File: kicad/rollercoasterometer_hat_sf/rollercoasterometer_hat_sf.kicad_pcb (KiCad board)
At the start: 2 copper layers, 65 x 87.8 mm, 66 parts, among them J101 Raspberry_Pi_40, J102 Conn_01x03, J103 LSD9DS1, J104 ICM20948, J105 BME680, J201 SMA, J202 NormallyClosed, J301 USB_C_Receptacle, J302 USB_C_Receptacle, U1201 LPC2103, U1401 74LS138, U1402 TXS0108, U1601 ICM-42688, U1701 BMM150, U1801 AK09918, U1901 BMP384, U201 ZED_F9R, U401 TCR2EF 3.3V, U501 TCR2EF 1.8V, Y1201 12MHz

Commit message: Commit as-ordered shipometer 23.03
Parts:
- removed C1605: 10nF, Capacitor_SMD:C_0402_1005Metric
- removed C1606: 2.2uF, Capacitor_SMD:C_0402_1005Metric
- removed C1608, C1722, C1755, C1811, C1901, C1910: 100nF, Capacitor_SMD:C_0402_1005Metric
- removed D302: RED, LED_SMD:LED_0603_1608Metric
- removed G1501: Axis, KwanSystems:Axis
- removed G1502, G1505: KwanSystems, KwanSystems:StKwansSoldermask
- removed G1503, G1507: DesignedWithKicad, KwanSystems:Symbol_KiCAD-Logo_CopperAndSilkScreenTop_small
- removed G1504, G1506: OSHW, KwanSystems:OSHW-Symbol_6.7x6mm_SolderMask
- removed J302: USB_C_Receptacle, KwanSystems:USB_C_Amphenol_MidMount_with_cutout
- removed U1402: TXS0108, Package_SO:TSSOP-20_4.4x6.5mm_P0.65mm
- removed U1601: ICM-42688, KwanSystems:QFN50P300X250X97-14N
- removed U1701: BMM150, KwanSystems:BMM150
- removed U1801: AK09918, KwanSystems:AK09918C
- removed U1901: BMP384, KwanSystems:BMP384
- added D101: White, LED_SMD:LED_0603_1608Metric, F.Cu at (208.0, 55.9)
- added D102: White, LED_SMD:LED_0603_1608Metric, F.Cu at (208.0, 57.7)
- added D103: White, LED_SMD:LED_0603_1608Metric, F.Cu at (208.0, 59.4)
- added D104: White, LED_SMD:LED_0603_1608Metric, F.Cu at (208.0, 61.2)
- added D1206: Blue, LED_SMD:LED_0603_1608Metric, F.Cu at (208.0, 64.8)
- added D1229: Red, LED_SMD:LED_0603_1608Metric, F.Cu at (208.0, 70.1)
- added D1230: Green, LED_SMD:LED_0603_1608Metric, F.Cu at (208.0, 68.3)
- added D1241: Yellow, LED_SMD:LED_0603_1608Metric, F.Cu at (208.0, 63.0)
- added D1244: Yellow, LED_SMD:LED_0603_1608Metric, F.Cu at (208.0, 66.5)
- added R1229: 68, Resistor_SMD:R_0402_1005Metric, F.Cu at (201.7, 71.4)
- added R1241: 68, Resistor_SMD:R_0402_1005Metric, F.Cu at (201.7, 63.0)
- added R1244: 68, Resistor_SMD:R_0402_1005Metric, F.Cu at (201.7, 68.3)
- D301: value RED -> USBLC6-4SC6; footprint LED_SMD:LED_0603_1608Metric -> Package_TO_SOT_SMD:SOT-23-6
- G103, G107: value DesignedWithKicad -> Designed with
- J103: value LSD9DS1 -> LSM9DS1
- J202: footprint KwanSystems:SolderJumper-2_P1.3mm_MaskBridged_RoundedPad1.0x1.5mm -> Jumper:SolderJumper-2_P1.3mm_Bridged_RoundedPad1.0x1.5mm
- moved U102 38.9 mm to (159.3, 59.2)
- moved C401 19.8 mm to (177.4, 70.2), turned to 90 degrees
- moved U401 17.5 mm to (174.6, 70.2), turned to 180 degrees
- moved C405 15.8 mm to (171.8, 70.2), turned to 90 degrees
- moved D301 8.76 mm to (177.5, 87.9), turned to -90 degrees
- moved R302 2.03 mm to (175.5, 92.2)
- moved C1240 0.79 mm to (163.6, 58.4)
- moved G103 0.36 mm to (208.5, 93.5)
- moved G107 0.36 mm to (208.5, 93.5)
- renumbered U1401 to U102
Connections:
- C1217 pad 1: +1V8 -> +3V3
- C1240 pad 1: +1V8 -> +3V3
- D301 pad 1: GND -> unconnected-(D301-Pad1)
- D301 pad 2: /P_RET_1V8 -> GND
- J101 pad 10: /GPS_TX -> /LPC_TX
- J101 pad 11: /LPC_~{RESET} -> /CS_A2
- J101 pad 13: unconnected-(J101-Pad13) -> /CS_A1
- J101 pad 15: unconnected-(J101-Pad15) -> /CS_A0
- J101 pad 16: unconnected-(J101-Pad16) -> /LPC_~{RESET}
- J101 pad 18: unconnected-(J101-Pad18) -> /LPC_~{BOOTSTRAP}
- J101 pad 22: unconnected-(J101-Pad22) -> /DRDY_MAG
- J101 pad 29: unconnected-(J101-Pad29) -> /GPS_RX
- J101 pad 31: unconnected-(J101-Pad31) -> /DRDY_6D
- J101 pad 32: /LPC_RX -> unconnected-(J101-Pad32)
- J101 pad 33: /LPC_TX -> unconnected-(J101-Pad33)
- J101 pad 35: /CS1 -> unconnected-(J101-Pad35)
- J101 pad 37: /CS0 -> unconnected-(J101-Pad37)
- J101 pad 7: unconnected-(J101-Pad7) -> /GPS_TX
- J101 pad 8: /GPS_RX -> /LPC_RX
- J301 pad A11: /USB+ Cable/P_INT2 -> unconnected-(J301-PadA11)
- J301 pad A2: /SDA_LPC_1V8 -> unconnected-(J301-PadA2)
- J301 pad A5: /USB+ Cable/P_CC1 -> /USB C Cable/P_CC1
- J301 pad A8: +1V8 -> unconnected-(J301-PadA8)
- J301 pad B10: /SCL_LPC_1V8 -> unconnected-(J301-PadB10)
- J301 pad B11: /P_RET_1V8 -> unconnected-(J301-PadB11)
- J301 pad B2: /USB+ Cable/P_INT3 -> unconnected-(J301-PadB2)
- J301 pad B3: /SHOE_INT_1V8 -> unconnected-(J301-PadB3)
- J301 pad B5: /USB+ Cable/P_CC2 -> /USB C Cable/P_CC2
- J301 pad S1: GND -> unconnected-(J301-PadS1)
- R301 pad 2: /USB+ Cable/P_CC2 -> /USB C Cable/P_CC1
- R302 pad 2: /USB+ Cable/P_CC1 -> /USB C Cable/P_CC2
- U102 pad 1: /CS0 -> /CS_A0
- U102 pad 2: /CS1 -> /CS_A1
- U102 pad 3: GND -> /CS_A2
- U1201 pad 10: /Timer/CAP2.2 -> unconnected-(U1201-Pad10)
- U1201 pad 18: /SCL_LPC_3V3 -> /Timer/SCL0
- U1201 pad 21: /SDA_LPC_3V3 -> /Timer/SDA0
- U1201 pad 29: unconnected-(U1201-Pad29) -> /Timer/DRDY
- U1201 pad 30: unconnected-(U1201-Pad30) -> /Timer/DRDY_MAG_ECHO
- U1201 pad 4: +1V8 -> +3V3
- U1201 pad 41: unconnected-(U1201-Pad41) -> /Timer/PPS-
- U1201 pad 44: /Timer/~{BOOTSTRAP} -> /LPC_~{BOOTSTRAP}
- U1201 pad 48: /SHOE_INT_3V3 -> /Timer/CAP1.3
- U1201 pad 8: /PPS -> unconnected-(U1201-Pad8)
- U1201 pad 9: /Timer/CAP2.1 -> unconnected-(U1201-Pad9)
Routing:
- net +3V3: track 40.5 -> 210.7 mm, vias 4 -> 6
- net /~{CS}_6D: track 0.00 -> 96.8 mm, vias 0 -> 5
- net /MOSI_3V3: track 0.00 -> 95.6 mm, vias 0 -> 3
- net /MISO_3V3: track 0.00 -> 84.9 mm, vias 0 -> 1
- net /~{CS}_MAG: track 0.00 -> 83.7 mm, vias 0 -> 2
- net /SCK_3V3: track 0.00 -> 79.0 mm
- net /LPC_~{RESET}: track 0.00 -> 68.6 mm, vias 0 -> 4
- net /VBUS: track 0.00 -> 66.4 mm, vias 0 -> 5
- net /DRDY_6D: track 0.00 -> 63.0 mm, vias 0 -> 6
- net /DRDY_MAG: track 0.00 -> 60.8 mm, vias 0 -> 3
- net /~{CS}_LPC_3V3: track 0.00 -> 58.6 mm, vias 0 -> 8
- net /LPC_~{BOOTSTRAP}: track 0.00 -> 57.4 mm, vias 0 -> 4
- net /~{CS}_PRES: track 0.00 -> 56.3 mm, vias 0 -> 6
- net /Q_1V8: track 53.5 -> 0.00 mm, vias 2 -> 0
- net /Timer/DRDY_MAG_ECHO: track 0.00 -> 46.5 mm, vias 0 -> 8
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- removed copper zone on B.Cu, net /Q_GND
- removed copper zone on F.Cu, net /Q_GND
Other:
- board size 65 x 87.8 mm -> 65 x 56.5 mm
- board text added: "03 Mar 2023"
- board text added: "Shipometer HAT"
- board text added: "Version 23.03 No Shoe"
- board text removed: "01 Nov 2022"
- board text removed: "Rollercoasterometer HAT"
- board text removed: "Rollercoasterometer Shoe"
- board text removed: "Shoe"
- board text removed: "Version 22.11"
- board text removed: "Version 22.11 01 Nov 2022"

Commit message: Improved grounding and bypass caps on GPS
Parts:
- added C233: 1uF, Capacitor_SMD:C_0402_1005Metric, F.Cu at (166.6, 71.9)
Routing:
- net /Timer/DRDY_MAG_ECHO: track 46.5 -> 56.1 mm, vias 8 -> 9
- net +3V3: track 210.7 -> 212.3 mm
- net /Timer/PPS-: track 41.2 -> 41.9 mm
- net /SCK_3V3: track 79.0 -> 79.6 mm
- net GND: vias 55 -> 62

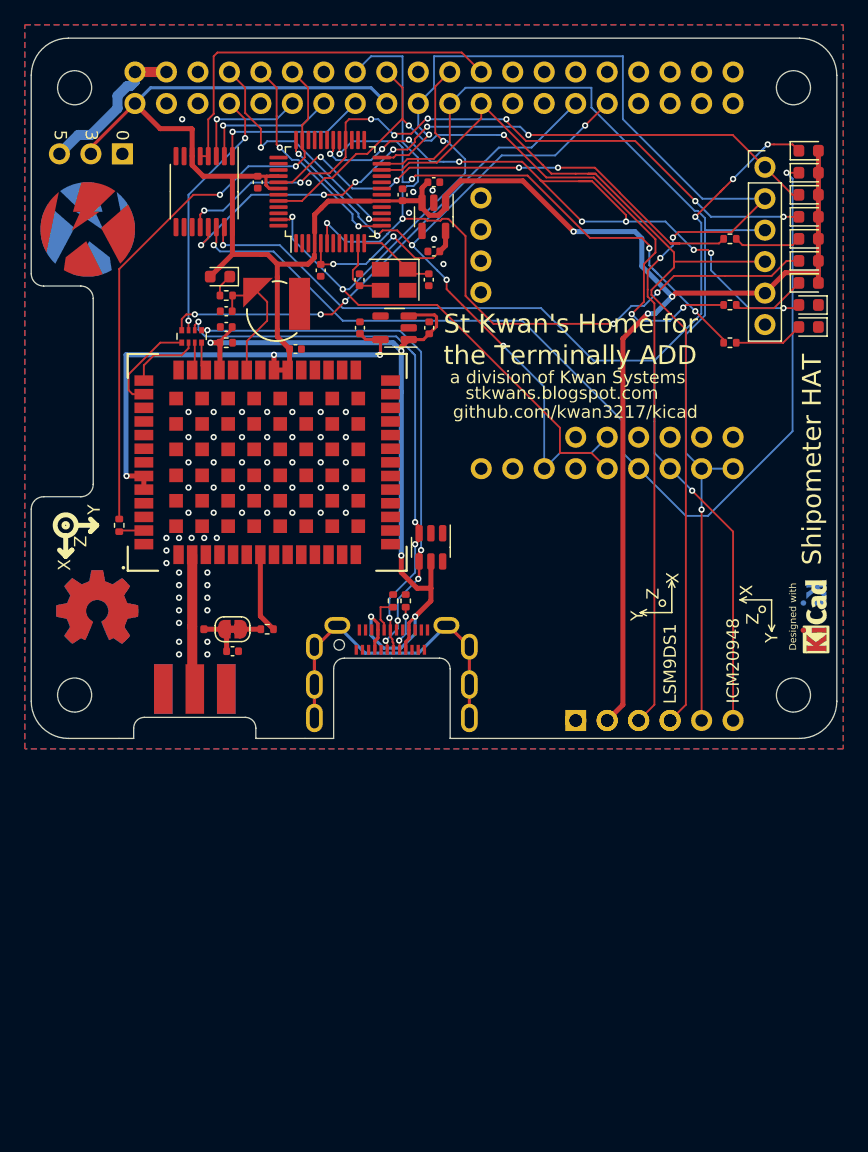
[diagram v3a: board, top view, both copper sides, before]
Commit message: Added BME280 and ICM20948 stamps
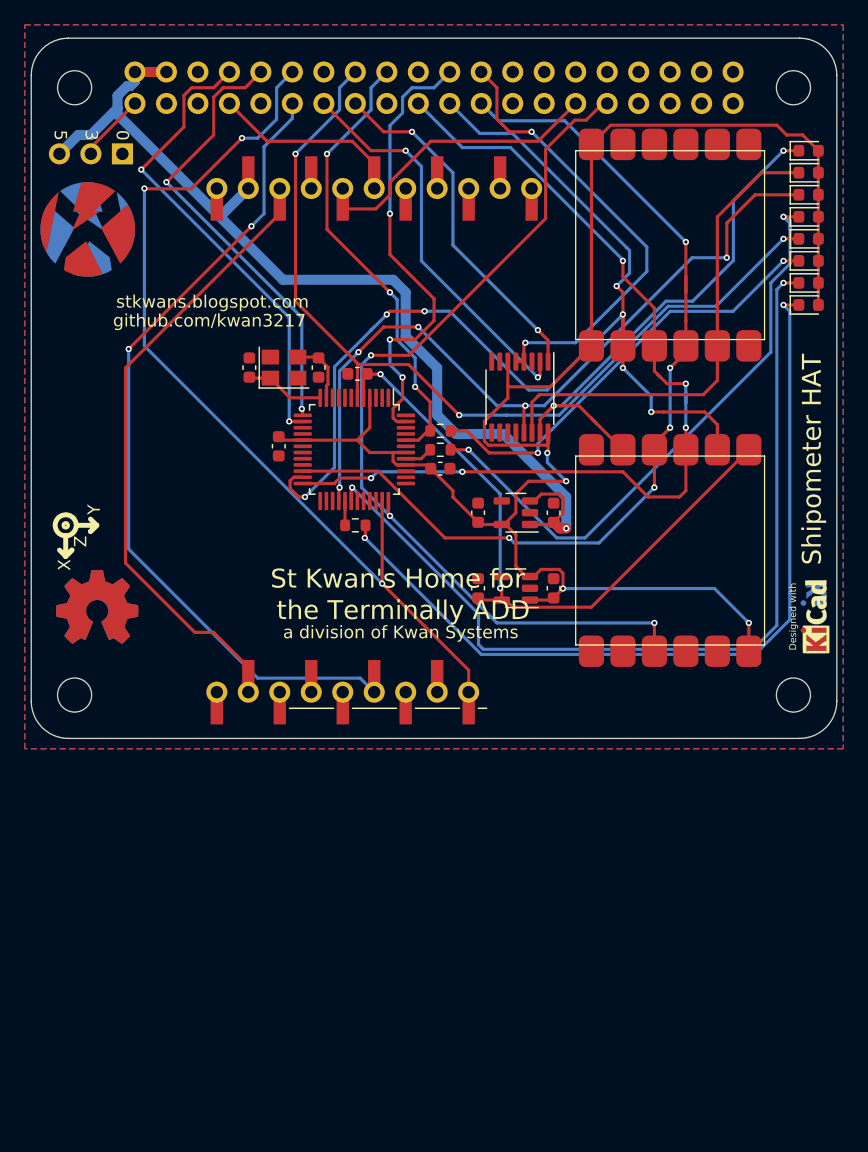
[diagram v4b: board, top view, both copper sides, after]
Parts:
- removed B201: ML414H, KwanSystems:Coin_Cell_ML414H
- removed C201: 47pF, Capacitor_SMD:C_0402_1005Metric
- removed C233, C236, C238: 1uF, Capacitor_SMD:C_0402_1005Metric
- removed D102: White, LED_SMD:LED_0603_1608Metric
- removed D201: 0.5A/420mV, Diode_SMD:D_0603_1608Metric
- removed D301: USBLC6-4SC6, Package_TO_SOT_SMD:SOT-23-6
- removed J103: LSM9DS1, SparkfunBreakout:LSM9DS1
- removed J201: SMA, KwanSystems:SMA-EDGE
- removed J202: NormallyClosed, Jumper:SolderJumper-2_P1.3mm_Bridged_RoundedPad1.0x1.5mm
- removed J301: USB_C_Receptacle, KwanSystems:USB_C_Amphenol_MidMount_with_cutout
- removed L201: Ferrite 120NH, Inductor_SMD:L_0402_1005Metric
- removed R1229, R1241, R1244: 68, Resistor_SMD:R_0402_1005Metric
- removed R238: 100k, Resistor_SMD:R_0402_1005Metric
- removed R239: 27, KwanSystems:R_Array_Convex_4x0402
- removed R253, R407: 27, Resistor_SMD:R_0402_1005Metric
- removed R301, R302, R436: 5.1k, Resistor_SMD:R_0402_1005Metric
- removed U201: ZED_F9R, KwanSystems:ZED-F9x
- added J106: ZED-F9R, SparkfunBreakout:ZED-F9R, F.Cu at (146.3, 100.8)
- added R1: 68, Resistor_SMD:R_0603_1608Metric, F.Cu at (171.4, 86.1)
- added R144: 68, Resistor_SMD:R_0603_1608Metric, F.Cu at (178.3, 78.5)
- added R2: 68, Resistor_SMD:R_0603_1608Metric, F.Cu at (178.3, 80.0)
- C1205, C1211, C1212, C1217, C1240, C401, C405, C501, C505: footprint Capacitor_SMD:C_0402_1005Metric -> Capacitor_SMD:C_0603_1608Metric
- J104: footprint SparkfunBreakout:ICM20948 -> KwanSystems:StampPad
- J105: value BME680 -> BME280; footprint SparkfunBreakout:BME680 -> KwanSystems:StampPad
- moved C501 34.2 mm to (187.5, 91.2), turned to 90 degrees
- moved U501 30.7 mm to (184.4, 91.2), turned to 180 degrees
- moved U102 30.4 mm to (184.7, 75.8)
- moved C505 27.4 mm to (181.4, 91.2), turned to 90 degrees
- moved C1240 27.4 mm to (178.3, 81.5), turned to 0 degrees
- moved C1217 22.6 mm to (165.3, 79.7), turned to -90 degrees
- moved U1201 20.9 mm to (171.4, 80.0), turned to -90 degrees
- moved C401 18.0 mm to (187.5, 85.1)
- moved U401 17.8 mm to (184.4, 85.1)
- moved C405 17.7 mm to (181.4, 85.1)
- moved J105 17.3 mm to (196.8, 63.5), turned to 90 degrees
- moved C1212 16.1 mm to (162.9, 73.4), turned to -90 degrees
- moved J104 15.5 mm to (196.8, 88.1), turned to -90 degrees
- moved Y1201 11.4 mm to (165.7, 73.4), turned to 0 degrees
- moved C1205 8.87 mm to (171.6, 73.9), turned to 180 degrees
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- renumbered D1206 to D106, D1229 to D129, D1230 to D130, D1241 to D141, D1244 to D144
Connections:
- C401 pad 1: /VBUS -> +5V
- D129 pad 1: GND -> /DRDY-
- D129 pad 2: /Timer/DRDY_6D_ECHO+ -> +3V3
- D130 pad 1: GND -> /~{DRDY}_MAG_ECHO
- D130 pad 2: /Timer/DRDY_MAG_ECHO -> +3V3
- D141 pad 1: /Timer/PPS+ -> Net-(D141-K)
- D144 pad 1: /Timer/BOOSTSTRAP- -> Net-(D144-K)
- J101 pad 1: +3V3 -> +3.3VP
- J101 pad 11: /CS_A2 -> /GPS_~{RESET}
- J101 pad 17: +3V3 -> unconnected-(J101-3V3-Pad17)
- J102 pad 2: +3V3 -> +3.3VP
- J104 pad 1: GND -> +1V8
- J104 pad 11: /DRDY_6D -> unconnected-(J104-SCL-Pad11)
- J104 pad 12: GND -> +3V3
- J104 pad 2: +3V3 -> /MISO_3V3
- J104 pad 5: /MISO_3V3 -> /~{CS}_6D
- J104 pad 6: /~{CS}_6D -> GND
- J104 pad 7: unconnected-(J104-VIN-Pad7) -> GND
- J104 pad 9: unconnected-(J104-ADA-Pad9) -> /DRDY_6D
- J105 pad 1: unconnected-(J105-GND-Pad1) -> +3V3
- J105 pad 10: /~{CS}_PRES -> unconnected-(J105-Pad10)
- J105 pad 2: unconnected-(J105-3V3-Pad2) -> /MISO_3V3
- J105 pad 3: unconnected-(J105-SDA-Pad3) -> /MOSI_3V3
- J105 pad 4: unconnected-(J105-SCL-Pad4) -> /SCK_3V3
- J105 pad 5: GND -> /~{CS}_PRES
- J105 pad 6: +3V3 -> GND
- J105 pad 7: /SCK_3V3 -> GND
- J105 pad 8: /MISO_3V3 -> unconnected-(J105-Pad8)
- J105 pad 9: /MOSI_3V3 -> unconnected-(J105-Pad9)
- U102 pad 12: /~{CS}_LPC_3V3 -> unconnected-(U102-O3-Pad12)
- U102 pad 13: /~{CS}_PRES -> /~{CS}_LPC_3V3
- U102 pad 14: /~{CS}_MAG -> /~{CS}_PRES
- U102 pad 3: /CS_A2 -> GND
- U1201 pad 29: /Timer/DRDY -> /~{DRDY}_6D_ECHO
- U1201 pad 30: /Timer/DRDY_MAG_ECHO -> /~{DRDY}_MAG_ECHO
- U1201 pad 41: /Timer/PPS- -> /Timer/PPS_ECHO
- U401 pad 1: /VBUS -> +5V
- U401 pad 3: /VBUS -> +5V
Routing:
- net /~{CS}_MAG: track 83.7 -> 0.00 mm, vias 2 -> 0
- net +3V3: track 212.3 -> 139.9 mm, vias 6 -> 4
- net /~{DRDY}_MAG_ECHO: track 0.00 -> 72.1 mm, vias 0 -> 2
- net +5V: track 15.0 -> 83.0 mm, vias 0 -> 1
- net /DRDY-: track 0.00 -> 67.2 mm, vias 0 -> 2
- net /VBUS: track 66.4 -> 0.00 mm, vias 5 -> 0
- net /GPS_~{RESET}: track 0.00 -> 66.0 mm, vias 0 -> 2
- net /Timer/DRDY_MAG_ECHO: track 56.1 -> 0.00 mm, vias 9 -> 0
- net /~{CS}_6D: track 96.9 -> 42.8 mm, vias 5 -> 2
- net Net-(D141-K): track 0.00 -> 49.2 mm, vias 0 -> 2
- net 3V3: track 0.00 -> 48.1 mm
- net /D+: track 45.2 -> 0.00 mm, vias 4 -> 0
- net /D-: track 44.5 -> 0.00 mm, vias 5 -> 0
- net /Timer/DRDY: track 42.9 -> 0.00 mm, vias 4 -> 0
- net /Timer/PPS-: track 41.9 -> 0.00 mm, vias 4 -> 0
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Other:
- outline, holes or cut-outs redrawn
- board text added: "01 Apr 2023"
- board text added: "Version 23.04 No Shoe"
- board text removed: "03 Mar 2023"
- board text removed: "Version 23.03 No Shoe"

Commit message: Rotate IMU stamp to match GPS
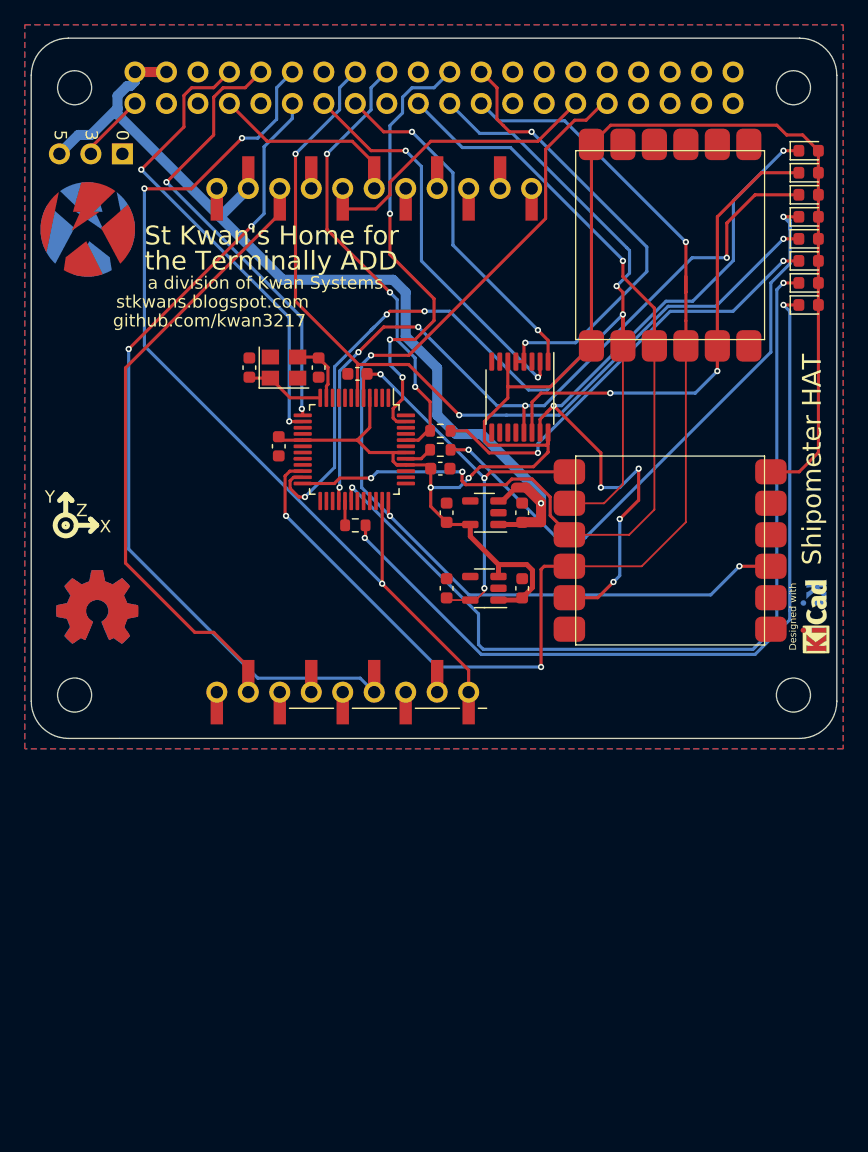
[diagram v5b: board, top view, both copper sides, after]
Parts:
- moved C401 2.54 mm to (184.9, 85.1)
- moved C405 2.54 mm to (178.8, 85.1)
- moved C501 2.54 mm to (184.9, 91.2)
- moved C505 2.54 mm to (178.8, 91.2)
- moved U401 2.54 mm to (181.9, 85.1)
- moved U501 2.54 mm to (181.9, 91.2)
- turned G101 to 0 degrees
- turned J104 to 0 degrees
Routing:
- net /SCK_3V3: track 75.9 -> 96.6 mm, vias 5 -> 3
- net /~{CS}_6D: track 42.8 -> 61.1 mm, vias 2 -> 6
- net +1V8: track 52.8 -> 34.6 mm, vias 2 -> 3
- net /DRDY_6D: track 73.4 -> 80.5 mm
- net +3V3: track 139.9 -> 136.7 mm, vias 4 -> 2
- net +5V: track 83.0 -> 80.1 mm
- net /MISO_3V3: track 90.2 -> 92.3 mm, vias 7 -> 5
- net /MOSI_3V3: track 76.8 -> 76.3 mm, vias 5 -> 3
- net /~{CS}_PRES: track 39.4 -> 38.9 mm, vias 0 -> 2
